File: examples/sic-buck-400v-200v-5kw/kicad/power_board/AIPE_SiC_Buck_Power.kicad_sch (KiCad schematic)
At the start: 0 parts

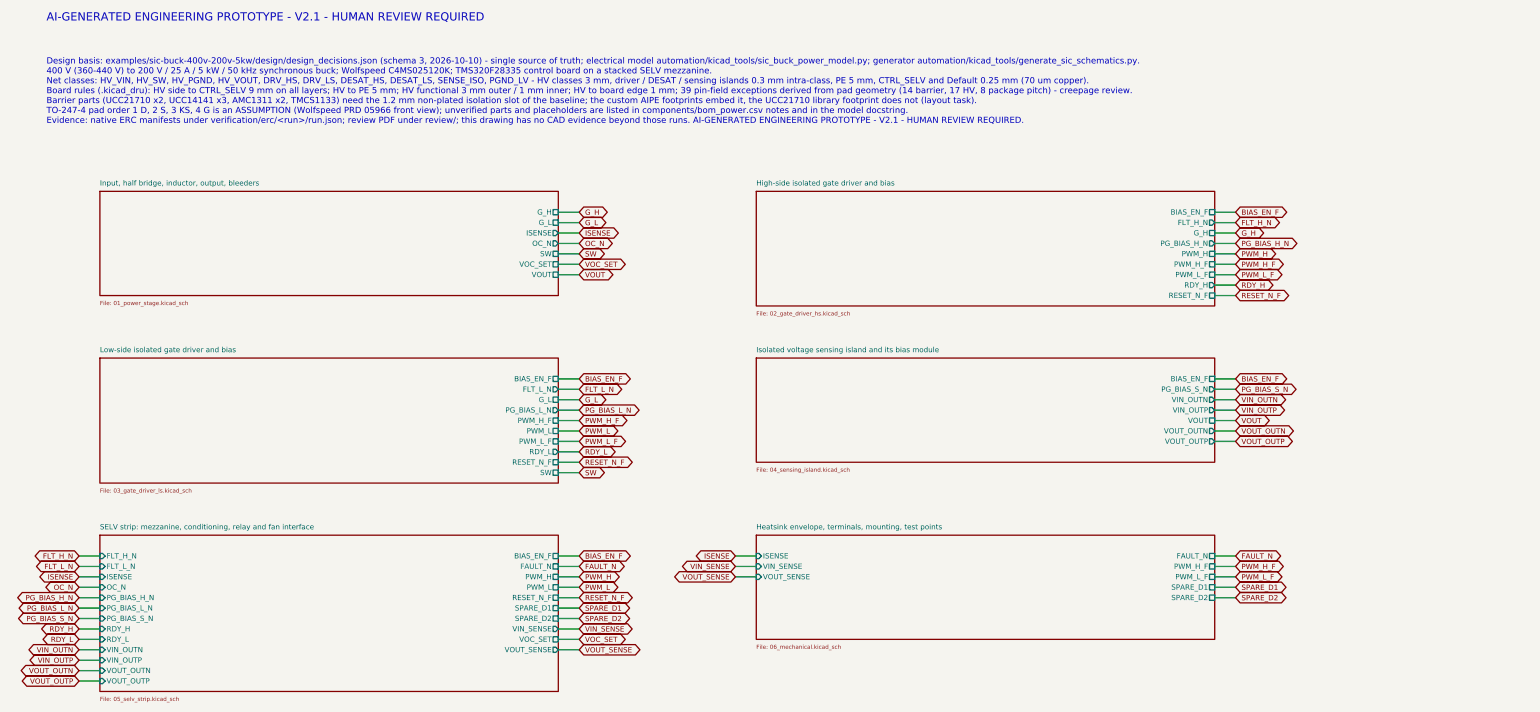
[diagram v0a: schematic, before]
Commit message: Correct sensing circuits and add verified V2.2 local bypasses
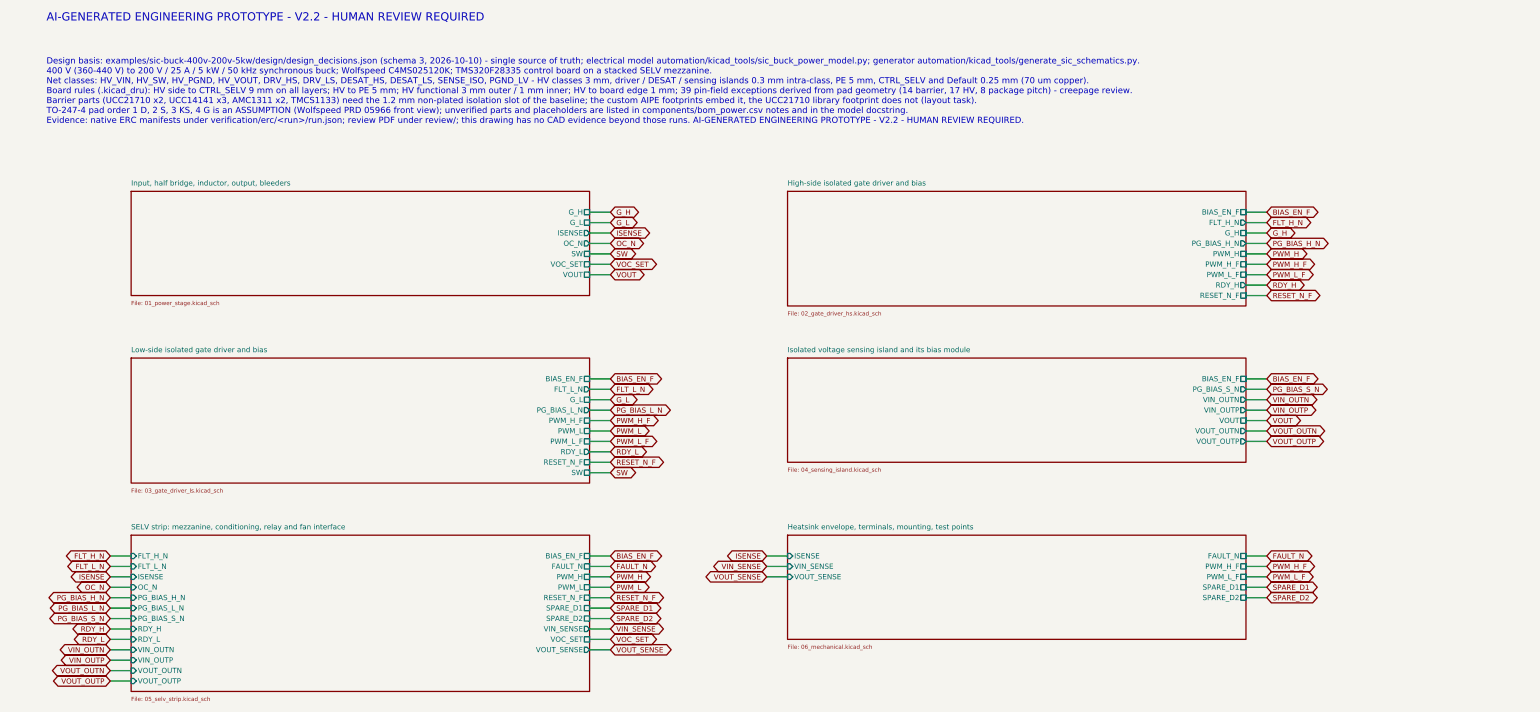
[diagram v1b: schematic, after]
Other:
- note added: "AI-GENERATED ENGINEERING PROTOTYPE - V2.2 - HUMAN REVIEW REQUIRED"
- note removed: "AI-GENERATED ENGINEERING PROTOTYPE - V2.1 - HUMAN REVIEW REQUIRED"
- title: AIPE V2 SiC buck power board - 400 V (360-440 V) to 200 V / 25 A / 5 kW / 50 kHz synchronous buck; Wolfspeed C4MS025120K; TMS320F28335 control board on a stacked SELV mezzanine -> SiC buck 400V / 200V / 5kW - power board
